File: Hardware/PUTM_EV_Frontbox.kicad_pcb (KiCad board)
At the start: 2 copper layers, 60 x 40 mm, 4 parts

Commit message: Initial layout, changes in safety sensing bus labels
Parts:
- added C1: 22uF, Capacitor_SMD:CP_Elec_4x5.8, F.Cu at (136.1, 99.9)
- added C10: 22uF, Capacitor_SMD:C_0805_2012Metric, F.Cu at (132.1, 116.9)
- added C11: 1uF, Capacitor_SMD:C_0603_1608Metric_Pad1.08x0.95mm_HandSolder, F.Cu at (141.6, 119.4)
- added C12: 1uF, Capacitor_SMD:C_0603_1608Metric_Pad1.08x0.95mm_HandSolder, F.Cu at (150.6, 119.4)
- added C13: 1uF, Capacitor_SMD:C_0603_1608Metric_Pad1.08x0.95mm_HandSolder, F.Cu at (151.1, 115.4)
- added C14: 1uF, Capacitor_SMD:C_0603_1608Metric_Pad1.08x0.95mm_HandSolder, F.Cu at (152.5, 108.4)
- added C15: 1uF, Capacitor_SMD:C_0603_1608Metric_Pad1.08x0.95mm_HandSolder, F.Cu at (156.1, 108.4)
- added C16: 1uF, Capacitor_SMD:C_0603_1608Metric_Pad1.08x0.95mm_HandSolder, F.Cu at (156.1, 115.4)
- added C17: 1uF, Capacitor_SMD:C_0603_1608Metric_Pad1.08x0.95mm_HandSolder, F.Cu at (147.0, 106.4)
- added C18: 1uF, Capacitor_SMD:C_0603_1608Metric_Pad1.08x0.95mm_HandSolder, F.Cu at (158.6, 105.4)
- added C19: 10u, Capacitor_SMD:C_0805_2012Metric_Pad1.18x1.45mm_HandSolder, F.Cu at (99.9, 138.8)
- added C2: 22uF, Capacitor_SMD:CP_Elec_4x5.8, F.Cu at (136.1, 105.4)
- added C20: 100nF, Capacitor_SMD:C_0603_1608Metric_Pad1.08x0.95mm_HandSolder, F.Cu at (117.9, 127.3)
- added C21: 100nF, Capacitor_SMD:C_0603_1608Metric_Pad1.08x0.95mm_HandSolder, F.Cu at (118.0, 140.8)
- added C22: 100nF, Capacitor_SMD:C_0603_1608Metric_Pad1.08x0.95mm_HandSolder, F.Cu at (115.0, 141.3)
- added C23: 100nF, Capacitor_SMD:C_0603_1608Metric_Pad1.08x0.95mm_HandSolder, F.Cu at (103.9, 139.8)
- added C24: 100nF, Capacitor_SMD:C_0603_1608Metric_Pad1.08x0.95mm_HandSolder, F.Cu at (102.9, 126.3)
- added C25: 100nF, Capacitor_SMD:C_0603_1608Metric_Pad1.08x0.95mm_HandSolder, F.Cu at (102.9, 124.3)
- added C26: 100nF, Capacitor_SMD:C_0603_1608Metric_Pad1.08x0.95mm_HandSolder, F.Cu at (110.5, 123.4)
- added C27: 100n, Capacitor_SMD:C_0603_1608Metric, F.Cu at (121.0, 132.1)
- added C28: 100nF, Capacitor_SMD:C_0603_1608Metric_Pad1.08x0.95mm_HandSolder, F.Cu at (123.3, 139.3)
- added C29: 6p, Capacitor_SMD:C_0603_1608Metric_Pad1.08x0.95mm_HandSolder, F.Cu at (119.8, 139.3)
- added C3: 100nF, Capacitor_SMD:C_0603_1608Metric, F.Cu at (137.6, 113.9)
- added C30: 100n, Capacitor_SMD:C_0603_1608Metric_Pad1.08x0.95mm_HandSolder, F.Cu at (100.8, 118.8)
- added C31: 100n, Capacitor_SMD:C_0603_1608Metric_Pad1.08x0.95mm_HandSolder, F.Cu at (108.6, 118.8)
- added C32: 47u, Capacitor_SMD:C_0603_1608Metric_Pad1.08x0.95mm_HandSolder, F.Cu at (100.8, 116.8)
- added C33: 10n, Capacitor_SMD:C_0603_1608Metric_Pad1.08x0.95mm_HandSolder, F.Cu at (108.6, 116.8)
- added C34: 47u, Capacitor_SMD:C_0603_1608Metric_Pad1.08x0.95mm_HandSolder, F.Cu at (106.1, 100.8)
- added C35: 220n, Capacitor_SMD:C_0603_1608Metric_Pad1.08x0.95mm_HandSolder, F.Cu at (102.8, 102.8)
- added C36: 100n, Capacitor_SMD:C_0603_1608Metric_Pad1.08x0.95mm_HandSolder, F.Cu at (108.8, 101.8)
- added C37: 10n, Capacitor_SMD:C_0603_1608Metric_Pad1.08x0.95mm_HandSolder, F.Cu at (106.1, 98.8)
- added C38: 100n, Capacitor_SMD:C_0603_1608Metric_Pad1.08x0.95mm_HandSolder, F.Cu at (117.7, 118.7)
- added C39: 100n, Capacitor_SMD:C_0603_1608Metric_Pad1.08x0.95mm_HandSolder, F.Cu at (124.7, 118.7)
- added C4: 22uF, Capacitor_SMD:C_0805_2012Metric, F.Cu at (142.6, 104.9)
- added C40: 47u, Capacitor_SMD:C_0603_1608Metric_Pad1.08x0.95mm_HandSolder, F.Cu at (117.7, 116.7)
- added C41: 10n, Capacitor_SMD:C_0603_1608Metric_Pad1.08x0.95mm_HandSolder, F.Cu at (124.7, 116.7)
- added C42: 47u, Capacitor_SMD:C_0603_1608Metric_Pad1.08x0.95mm_HandSolder, F.Cu at (122.0, 100.7)
- added C43: 220n, Capacitor_SMD:C_0603_1608Metric_Pad1.08x0.95mm_HandSolder, F.Cu at (118.5, 102.7)
- added C44: 100n, Capacitor_SMD:C_0603_1608Metric_Pad1.08x0.95mm_HandSolder, F.Cu at (124.7, 101.7)
- added C45: 10n, Capacitor_SMD:C_0603_1608Metric_Pad1.08x0.95mm_HandSolder, F.Cu at (122.0, 98.7)
- added C46: 100n, Capacitor_SMD:C_0603_1608Metric_Pad1.08x0.95mm_HandSolder, F.Cu at (91.8, 106.4)
- added C47: 100n, Capacitor_SMD:C_0603_1608Metric_Pad1.08x0.95mm_HandSolder, F.Cu at (91.8, 108.4)
- added C48: 100n, Capacitor_SMD:C_0603_1608Metric_Pad1.08x0.95mm_HandSolder, F.Cu at (91.8, 112.4)
- added C49: 10n, Capacitor_SMD:C_0603_1608Metric_Pad1.08x0.95mm_HandSolder, F.Cu at (80.8, 109.4)
- added C5: 22uF, Capacitor_SMD:C_0805_2012Metric, F.Cu at (142.6, 106.9)
- added C50: 100n, Capacitor_SMD:C_0603_1608Metric_Pad1.08x0.95mm_HandSolder, F.Cu at (91.4, 118.4)
- added C51: 100n, Capacitor_SMD:C_0603_1608Metric_Pad1.08x0.95mm_HandSolder, F.Cu at (91.4, 120.4)
- added C52: 100n, Capacitor_SMD:C_0603_1608Metric_Pad1.08x0.95mm_HandSolder, F.Cu at (91.4, 124.4)
- added C53: 10n, Capacitor_SMD:C_0603_1608Metric_Pad1.08x0.95mm_HandSolder, F.Cu at (80.5, 121.4)
- added C54: 100n, Capacitor_SMD:C_0603_1608Metric_Pad1.08x0.95mm_HandSolder, F.Cu at (78.8, 135.8)
- added C55: 100n, Capacitor_SMD:C_0603_1608Metric_Pad1.08x0.95mm_HandSolder, F.Cu at (82.8, 128.8)
- added C56: 100n, Capacitor_SMD:C_0603_1608Metric_Pad1.08x0.95mm_HandSolder, F.Cu at (82.8, 135.8)
- added C57: 100n, Capacitor_SMD:C_0603_1608Metric_Pad1.08x0.95mm_HandSolder, F.Cu at (131.8, 142.4)
- added C58: 100n, Capacitor_SMD:C_0603_1608Metric_Pad1.08x0.95mm_HandSolder, F.Cu at (145.9, 142.5)
- added C59: 100n, Capacitor_SMD:C_0603_1608Metric_Pad1.08x0.95mm_HandSolder, F.Cu at (134.8, 142.4)
- added C6: 100nF, Capacitor_SMD:C_0603_1608Metric, F.Cu at (142.3, 108.9)
- added C60: 100n, Capacitor_SMD:C_0603_1608Metric_Pad1.08x0.95mm_HandSolder, F.Cu at (148.9, 142.5)
- added C61: 100n, Capacitor_SMD:C_0603_1608Metric_Pad1.08x0.95mm_HandSolder, F.Cu at (137.8, 142.4)
- added C62: 100n, Capacitor_SMD:C_0603_1608Metric_Pad1.08x0.95mm_HandSolder, F.Cu at (151.9, 142.5)
- added C63: 100n, Capacitor_SMD:C_0603_1608Metric_Pad1.08x0.95mm_HandSolder, F.Cu at (140.8, 142.4)
- added C64: 100n, Capacitor_SMD:C_0603_1608Metric_Pad1.08x0.95mm_HandSolder, F.Cu at (154.9, 142.5)
- added C65: 100n, Capacitor_SMD:C_0603_1608Metric_Pad1.08x0.95mm_HandSolder, F.Cu at (137.8, 147.6)
- added C7: 22uF, Capacitor_SMD:C_0805_2012Metric, F.Cu at (139.6, 116.9)
- added C8: 22uF, Capacitor_SMD:C_0805_2012Metric, F.Cu at (137.1, 116.9)
- added C9: 22uF, Capacitor_SMD:C_0805_2012Metric, F.Cu at (134.6, 116.9)
- added D1: NSVRB751V40T1G, Diode_SMD:D_SOD-323_HandSoldering, F.Cu at (136.2, 167.0)
- added D10: 30V, Diode_SMD:D_SOD-123, F.Cu at (153.1, 99.9)
- added D11: LED, LED_SMD:LED_0603_1608Metric_Pad1.05x0.95mm_HandSolder, F.Cu at (94.5, 134.3)
- added D12: LED, LED_SMD:LED_0603_1608Metric_Pad1.05x0.95mm_HandSolder, F.Cu at (94.5, 132.8)
- added D13: LED, LED_SMD:LED_0603_1608Metric_Pad1.05x0.95mm_HandSolder, F.Cu at (94.5, 131.3)
- added D14: LED, LED_SMD:LED_0603_1608Metric_Pad1.05x0.95mm_HandSolder, F.Cu at (94.5, 129.8)
- added D2: 3.6V/400W, Package_TO_SOT_SMD:SOT-23-6, F.Cu at (90.9, 146.7)
- added D3: BZX84C5V6, Package_TO_SOT_SMD:SOT-23, F.Cu at (142.3, 123.3)
- added D4: BZX84C3V6-E3-08, Package_TO_SOT_SMD:SOT-23, F.Cu at (153.3, 119.8)
- added D5: 3.6V/400W, Package_TO_SOT_SMD:SOT-23-6, F.Cu at (87.4, 95.8)
- added D6: 5.3V/400W, Package_TO_SOT_SMD:SOT-23-3, F.Cu at (93.8, 96.3)
- added D7: 5.3V/400W, Package_TO_SOT_SMD:SOT-23-3, F.Cu at (127.2, 99.7)
- added D8: 5.3V/400W, Package_TO_SOT_SMD:SOT-23-3, F.Cu at (111.3, 99.6)
- added D9: 10V, Diode_SMD:D_SOD-123, F.Cu at (141.6, 100.9)
- added F1: 1.5A, Fuse:Fuse_1812_4532Metric, F.Cu at (149.6, 99.4)
- added F2: 300mA, Fuse:Fuse_0603_1608Metric_Pad1.05x0.95mm_HandSolder, F.Cu at (143.6, 119.4)
- added F3: 300mA, Fuse:Fuse_0603_1608Metric_Pad1.05x0.95mm_HandSolder, F.Cu at (149.1, 115.4)
- added F4: 300mA, Fuse:Fuse_0603_1608Metric_Pad1.05x0.95mm_HandSolder, F.Cu at (154.1, 115.4)
- added F5: 300mA, Fuse:Fuse_0603_1608Metric_Pad1.05x0.95mm_HandSolder, F.Cu at (150.6, 106.4)
- added F6: 300mA, Fuse:Fuse_0603_1608Metric_Pad1.05x0.95mm_HandSolder, F.Cu at (134.0, 113.9)
- added FB1: 2K@100MHz, Inductor_SMD:L_0603_1608Metric_Pad1.05x0.95mm_HandSolder, F.Cu at (103.8, 117.8)
- added FB2: 2K@100MHz, Inductor_SMD:L_0603_1608Metric_Pad1.05x0.95mm_HandSolder, F.Cu at (105.8, 117.8)
- added FB3: 2K@100MHz, Inductor_SMD:L_0603_1608Metric_Pad1.05x0.95mm_HandSolder, F.Cu at (106.1, 102.8)
- added FB4: 2K@100MHz, Inductor_SMD:L_0603_1608Metric_Pad1.05x0.95mm_HandSolder, F.Cu at (102.8, 100.8)
- added FB5: 2K@100MHz, Inductor_SMD:L_0603_1608Metric_Pad1.05x0.95mm_HandSolder, F.Cu at (120.2, 117.7)
- added FB6: 2K@100MHz, Inductor_SMD:L_0603_1608Metric_Pad1.05x0.95mm_HandSolder, F.Cu at (122.2, 117.7)
- added FB7: 2K@100MHz, Inductor_SMD:L_0603_1608Metric_Pad1.05x0.95mm_HandSolder, F.Cu at (122.0, 102.7)
- added FB8: 2K@100MHz, Inductor_SMD:L_0603_1608Metric_Pad1.05x0.95mm_HandSolder, F.Cu at (118.5, 100.7)
- added IC1: TPS54202HDDCR, Package_TO_SOT_SMD:SOT-23-6, F.Cu at (138.2, 111.4)
- added J1: XIAO ESP32S3 Sense, Samacsys:XIAO-ESP32S3-DIP, F.Cu at (121.6, 174.6)
- added J2: Conn_02x16_Counter_Clockwise, Connector_IDC:IDC-Header_2x17-1MP_P2.54mm_Latch6.5mm_Vertical, F.Cu at (90.7, 89.0)
- added J3: FTSH-107-01-L-D-K, Samacsys:FTSH-107-XX-YYY-D-K, F.Cu at (99.7, 146.9)
- added JP1: Jumper_2_Small_Bridged, Jumper:SolderJumper-2_P1.3mm_Open_TrianglePad1.0x1.5mm, F.Cu at (117.5, 95.3)
- added JP2: Jumper_2_Small_Bridged, Jumper:SolderJumper-2_P1.3mm_Open_TrianglePad1.0x1.5mm, F.Cu at (123.0, 131.8)
- added L1: 68uH/1.4A, Inductor_SMD:L_TDK_VLS6045EX_VLS6045AF, F.Cu at (144.5, 113.5)
- added Q1: SI2347DS-T1-GE3, Package_TO_SOT_SMD:SOT-23-3, F.Cu at (145.1, 100.9)
- added R1: 100k, Resistor_SMD:R_0603_1608Metric_Pad0.98x0.95mm_HandSolder, F.Cu at (142.6, 97.4)
- added R10: 1K, Resistor_SMD:R_0603_1608Metric_Pad0.98x0.95mm_HandSolder, F.Cu at (98.5, 134.3)
- added R11: 1K, Resistor_SMD:R_0603_1608Metric_Pad0.98x0.95mm_HandSolder, F.Cu at (98.5, 132.8)
- added R12: 1K, Resistor_SMD:R_0603_1608Metric_Pad0.98x0.95mm_HandSolder, F.Cu at (98.5, 131.3)
- added R13: 1K, Resistor_SMD:R_0603_1608Metric_Pad0.98x0.95mm_HandSolder, F.Cu at (98.5, 129.8)
- added R14: 100K, Resistor_SMD:R_0603_1608Metric_Pad0.98x0.95mm_HandSolder, F.Cu at (113.3, 102.8)
- added R15: 100K, Resistor_SMD:R_0603_1608Metric_Pad0.98x0.95mm_HandSolder, F.Cu at (129.7, 102.7)
- added R16: 330R, Resistor_SMD:R_0603_1608Metric_Pad0.98x0.95mm_HandSolder, F.Cu at (91.3, 103.5)
- added R17: 100k, Resistor_SMD:R_0603_1608Metric_Pad0.98x0.95mm_HandSolder, F.Cu at (78.8, 109.4)
- added R18: 0R, Resistor_SMD:R_0603_1608Metric_Pad0.98x0.95mm_HandSolder, F.Cu at (89.3, 103.5)
- added R19: 1K, Resistor_SMD:R_0603_1608Metric_Pad0.98x0.95mm_HandSolder, F.Cu at (93.3, 103.5)
- added R2: 510k, Resistor_SMD:R_0603_1608Metric, F.Cu at (139.1, 108.9)
- added R20: 1K, Resistor_SMD:R_0603_1608Metric_Pad0.98x0.95mm_HandSolder, F.Cu at (91.8, 110.4)
- added R21: 1K, Resistor_SMD:R_0603_1608Metric_Pad0.98x0.95mm_HandSolder, F.Cu at (79.8, 104.4)
- added R22: 1k, Resistor_SMD:R_0603_1608Metric_Pad0.98x0.95mm_HandSolder, F.Cu at (79.8, 106.4)
- added R23: 300R, Resistor_SMD:R_0603_1608Metric_Pad0.98x0.95mm_HandSolder, F.Cu at (90.5, 115.4)
- added R24: 100k, Resistor_SMD:R_0603_1608Metric_Pad0.98x0.95mm_HandSolder, F.Cu at (78.5, 121.4)
- added R25: 0R, Resistor_SMD:R_0603_1608Metric_Pad0.98x0.95mm_HandSolder, F.Cu at (88.5, 115.4)
- added R26: 0R, Resistor_SMD:R_0603_1608Metric_Pad0.98x0.95mm_HandSolder, F.Cu at (92.5, 115.4)
- added R27: 1K, Resistor_SMD:R_0603_1608Metric_Pad0.98x0.95mm_HandSolder, F.Cu at (91.4, 122.4)
- added R28: 1K, Resistor_SMD:R_0603_1608Metric_Pad0.98x0.95mm_HandSolder, F.Cu at (79.5, 116.4)
- added R29: 1K, Resistor_SMD:R_0603_1608Metric_Pad0.98x0.95mm_HandSolder, F.Cu at (79.5, 118.4)
- added R3: 100k, Resistor_SMD:R_0603_1608Metric, F.Cu at (134.4, 112.4)
- added R30: 1K, Resistor_SMD:R_0603_1608Metric_Pad0.98x0.95mm_HandSolder, F.Cu at (78.8, 137.8)
- added R31: 100K, Resistor_SMD:R_0603_1608Metric_Pad0.98x0.95mm_HandSolder, F.Cu at (78.8, 139.8)
- added R32: 1K, Resistor_SMD:R_0603_1608Metric_Pad0.98x0.95mm_HandSolder, F.Cu at (82.8, 137.8)
- added R33: 100K, Resistor_SMD:R_0603_1608Metric_Pad0.98x0.95mm_HandSolder, F.Cu at (82.8, 139.8)
- added R34: 10k, Resistor_SMD:R_0603_1608Metric_Pad0.98x0.95mm_HandSolder, F.Cu at (131.8, 128.8)
- added R35: 10k, Resistor_SMD:R_0603_1608Metric_Pad0.98x0.95mm_HandSolder, F.Cu at (145.4, 129.0)
- added R36: 2k, Resistor_SMD:R_0603_1608Metric_Pad0.98x0.95mm_HandSolder, F.Cu at (130.3, 142.4)
- added R37: 2k, Resistor_SMD:R_0603_1608Metric_Pad0.98x0.95mm_HandSolder, F.Cu at (144.4, 142.5)
- added R38: 10k, Resistor_SMD:R_0603_1608Metric_Pad0.98x0.95mm_HandSolder, F.Cu at (134.3, 128.8)
- added R39: 10k, Resistor_SMD:R_0603_1608Metric_Pad0.98x0.95mm_HandSolder, F.Cu at (147.9, 129.0)
- added R4: 43k, Resistor_SMD:R_0603_1608Metric, F.Cu at (136.1, 108.9)
- added R40: 2k, Resistor_SMD:R_0603_1608Metric_Pad0.98x0.95mm_HandSolder, F.Cu at (133.3, 142.4)
- added R41: 2k, Resistor_SMD:R_0603_1608Metric_Pad0.98x0.95mm_HandSolder, F.Cu at (147.4, 142.5)
- added R42: 10k, Resistor_SMD:R_0603_1608Metric_Pad0.98x0.95mm_HandSolder, F.Cu at (136.8, 128.8)
- added R43: 10k, Resistor_SMD:R_0603_1608Metric_Pad0.98x0.95mm_HandSolder, F.Cu at (150.4, 129.0)
- added R44: 2k, Resistor_SMD:R_0603_1608Metric_Pad0.98x0.95mm_HandSolder, F.Cu at (136.3, 142.4)
- added R45: 2k, Resistor_SMD:R_0603_1608Metric_Pad0.98x0.95mm_HandSolder, F.Cu at (150.4, 142.5)
- added R46: 10k, Resistor_SMD:R_0603_1608Metric_Pad0.98x0.95mm_HandSolder, F.Cu at (139.3, 128.9)
- added R47: 10k, Resistor_SMD:R_0603_1608Metric_Pad0.98x0.95mm_HandSolder, F.Cu at (152.9, 129.0)
- added R48: 2k, Resistor_SMD:R_0603_1608Metric_Pad0.98x0.95mm_HandSolder, F.Cu at (139.2, 142.4)
- added R49: 2k, Resistor_SMD:R_0603_1608Metric_Pad0.98x0.95mm_HandSolder, F.Cu at (153.4, 142.5)
- added R5: 13.3k, Resistor_SMD:R_0603_1608Metric, F.Cu at (134.4, 110.9)
- added R50: 10k, Resistor_SMD:R_0603_1608Metric_Pad0.98x0.95mm_HandSolder, F.Cu at (149.8, 147.8)
- added R51: 2k, Resistor_SMD:R_0603_1608Metric_Pad0.98x0.95mm_HandSolder, F.Cu at (135.3, 147.6)
- added R6: 1k, Resistor_SMD:R_0603_1608Metric, F.Cu at (112.5, 123.4)
- added R7: 10k, Resistor_SMD:R_0603_1608Metric, F.Cu at (119.0, 132.1)
- added R8: 10k, Resistor_SMD:R_0603_1608Metric, F.Cu at (112.4, 142.3)
- added R9: 10k, Resistor_SMD:R_0603_1608Metric, F.Cu at (112.4, 144.3)
- added TP1: TestPoint_Small, TestPoint:TestPoint_THTPad_D1.0mm_Drill0.5mm, F.Cu at (139.6, 97.4)
- added TP10: APPS_MID, TestPoint:TestPoint_THTPad_D1.0mm_Drill0.5mm, F.Cu at (73.8, 133.3)
- added TP11: BRAKE_OUT, TestPoint:TestPoint_THTPad_D1.0mm_Drill0.5mm, F.Cu at (73.8, 130.3)
- added TP12: BRAKE_MID, TestPoint:TestPoint_THTPad_D1.0mm_Drill0.5mm, F.Cu at (87.8, 133.3)
- added TP13: BRAKE_OUT, TestPoint:TestPoint_THTPad_D1.0mm_Drill0.5mm, F.Cu at (87.8, 130.3)
- added TP2: TestPoint_Small, TestPoint:TestPoint_THTPad_D1.0mm_Drill0.5mm, F.Cu at (149.5, 108.4)
- added TP3: TestPoint_Small, TestPoint:TestPoint_THTPad_D1.0mm_Drill0.5mm, F.Cu at (114.9, 124.3)
- added TP4: APPS_P, TestPoint:TestPoint_THTPad_D1.0mm_Drill0.5mm, F.Cu at (75.8, 109.4)
- added TP5: APPS_OUT, TestPoint:TestPoint_THTPad_D1.0mm_Drill0.5mm, F.Cu at (95.8, 108.4)
- added TP6: APPS_N, TestPoint:TestPoint_THTPad_D1.0mm_Drill0.5mm, F.Cu at (75.8, 106.9)
- added TP7: APPS_P, TestPoint:TestPoint_THTPad_D1.0mm_Drill0.5mm, F.Cu at (75.5, 121.9)
- added TP8: APPS_OUT, TestPoint:TestPoint_THTPad_D1.0mm_Drill0.5mm, F.Cu at (95.5, 120.4)
- added TP9: APPS_N, TestPoint:TestPoint_THTPad_D1.0mm_Drill0.5mm, F.Cu at (75.5, 118.9)
- added U1: TLV743P, Package_TO_SOT_SMD:SOT-23-5_HandSoldering, F.Cu at (146.9, 119.5)
- added U10: MCP6N11-001E/SN, Package_SO:SOIC-8_3.9x4.9mm_P1.27mm, F.Cu at (85.5, 120.4)
- added U11: MCP6002-xSN, Package_SO:SOIC-8_3.9x4.9mm_P1.27mm, F.Cu at (80.8, 132.3)
- added U12: TLP291-4, Package_SO:SOIC-16_4.55x10.3mm_P1.27mm, F.Cu at (136.3, 135.8)
- added U13: TLP291-4, Package_SO:SOIC-16_4.55x10.3mm_P1.27mm, F.Cu at (150.3, 135.8)
- added U14: FODM217B, Package_SO:SOP-4_4.4x2.6mm_P1.27mm, F.Cu at (143.8, 147.8)
- added U2: TLV743P, Package_TO_SOT_SMD:SOT-23-5_HandSoldering, F.Cu at (151.2, 111.4)
- added U3: TLV743P, Package_TO_SOT_SMD:SOT-23-5_HandSoldering, F.Cu at (156.6, 111.5)
- added U4: TLV743P, Package_TO_SOT_SMD:SOT-23-5_HandSoldering, F.Cu at (154.9, 105.5)
- added U5: LM4040C33FTA, Package_TO_SOT_SMD:SOT-23, F.Cu at (107.4, 123.2)
- added U6: STM32G484RETx, Package_QFP:LQFP-64_10x10mm_P0.5mm, F.Cu at (110.0, 133.8)
- added U7: ADM3057ExRW, Package_SO:SOIC-20W_7.5x12.8mm_P1.27mm, F.Cu at (107.8, 109.8)
- added U8: ADM3057ExRW, Package_SO:SOIC-20W_7.5x12.8mm_P1.27mm, F.Cu at (123.7, 109.7)
- added U9: MCP6N11-001E/SN, Package_SO:SOIC-8_3.9x4.9mm_P1.27mm, F.Cu at (85.8, 108.4)
- added Y1: ATX-11-F-32.000MHZ-F05-T, Samacsys:ATX11F32000MHZF05T, F.Cu at (121.4, 136.0)
- moved REF** 105.1 mm to (81.2, 26.4)
- moved REF** 105.1 mm to (31.2, 56.4)
- moved REF** 105.1 mm to (31.2, 26.4)
- moved REF** 105.1 mm to (81.2, 56.4)
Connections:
- REF** pad 1: (no net) -> GND (x4)
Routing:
- net /CAN bus/GND_CAN_ISO2: track 0.00 -> 26.8 mm
- net /CAN bus/GND_CAN_ISO1: track 0.00 -> 24.3 mm
- net Net-(R20-Pad1): track 0.00 -> 15.1 mm
- net Net-(R27-Pad1): track 0.00 -> 14.9 mm
- net /APPS2_SUPPLY: track 0.00 -> 11.3 mm
- net /APPS1_SUPPLY: track 0.00 -> 11.2 mm
- net Net-(U11A-+): track 0.00 -> 10.4 mm
- net Net-(C43-Pad1): track 0.00 -> 9.58 mm
- net Net-(C35-Pad1): track 0.00 -> 9.54 mm
- net Net-(U11B-+): track 0.00 -> 8.68 mm
- net /APPS_POT_2: track 0.00 -> 8.64 mm
- net /DAC2_REF: track 0.00 -> 8.52 mm
- net /DAC1_REF: track 0.00 -> 8.52 mm
- net /APPS_POT_1: track 0.00 -> 8.38 mm
- net Net-(U7-VISOIN): track 0.00 -> 8.26 mm
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
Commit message: Initial routing (Piotruś proszę nie bij że brzydko)
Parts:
- added D15: 3.6V/400W, Package_TO_SOT_SMD:SOT-23-6, F.Cu at (93.5, 143.2)
- C30, C38: value 100n -> 47u; footprint Capacitor_SMD:C_0603_1608Metric_Pad1.08x0.95mm_HandSolder -> Capacitor_SMD:C_0805_2012Metric_Pad1.18x1.45mm_HandSolder
- C32, C34, C40, C42: footprint Capacitor_SMD:C_0603_1608Metric_Pad1.08x0.95mm_HandSolder -> Capacitor_SMD:C_0805_2012Metric_Pad1.18x1.45mm_HandSolder
- C35, C43: value 220n -> 47u; footprint Capacitor_SMD:C_0603_1608Metric_Pad1.08x0.95mm_HandSolder -> Capacitor_SMD:C_0805_2012Metric_Pad1.18x1.45mm_HandSolder
- D7, D8: value 5.3V/400W -> PESD5V0L2BT; footprint Package_TO_SOT_SMD:SOT-23-3 -> Package_TO_SOT_SMD:SOT-23_Handsoldering
- moved REF** 129.3 mm to (162.4, 157.0)
- moved REF** 107.3 mm to (68.5, 157.0)
- moved REF** 101.3 mm to (162.4, 86.9)
- moved C16 82.5 mm to (73.5, 116.1), turned to 180 degrees
- moved C18 80.9 mm to (83.0, 134.2), turned to 180 degrees
- moved F4 80.6 mm to (73.5, 114.1), turned to 0 degrees
- moved U4 79.2 mm to (82.3, 137.2)
- moved F5 79.2 mm to (78.0, 138.0)
- moved U3 79.2 mm to (77.5, 115.7), turned to -90 degrees
- moved C13 78.7 mm to (73.6, 101.7), turned to 180 degrees
- moved F3 77.1 mm to (73.6, 99.7), turned to 0 degrees
- moved C17 76.8 mm to (78.0, 140.0), turned to 0 degrees
- moved C15 75.9 mm to (80.5, 116.1), turned to 90 degrees
- moved U2 74.5 mm to (77.4, 101.2), turned to -90 degrees
- moved C14 72.3 mm to (80.5, 101.4), turned to 90 degrees
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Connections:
- net /MCU/UART_RX renamed /Connector/UART_RX
- net /MCU/UART_TX renamed /Connector/UART_TX
- D7 pad 1: /CAN bus/CAN2- -> /CAN bus/CAN2+
- D7 pad 2: /CAN bus/CAN2+ -> /CAN bus/CAN2-
- D8 pad 1: /CAN bus/CAN1- -> /CAN bus/CAN1+
- D8 pad 2: /CAN bus/CAN1+ -> /CAN bus/CAN1-
- J3 pad 13: unconnected-(J3-Pin_13-Pad13) -> /Connector/UART_RX_PROG
- J3 pad 14: unconnected-(J3-Pin_14-Pad14) -> /Connector/UART_TX_PROG
- U6 pad 30: unconnected-(U6-PB10-Pad30) -> /Connector/UART_RX_PROG
- U6 pad 9: unconnected-(U6-PC1-Pad9) -> /Connector/UART_TX_PROG
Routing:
- net +3.3V: track 2.05 -> 231.3 mm, vias 0 -> 12
- net +5V: track 2.19 -> 170.6 mm, vias 0 -> 8
- net /MCU/RIGHT_KILL_S: track 0.00 -> 84.7 mm, vias 0 -> 2
- net /Connector/RIGHT_KILL: track 0.00 -> 82.0 mm, vias 0 -> 1
- net /MCU/BSPD_S: track 0.00 -> 81.6 mm, vias 0 -> 2
- net /Connector/BSPD: track 0.00 -> 80.9 mm, vias 0 -> 1
- net /MCU/OVERTRAVEL_S: track 0.00 -> 80.8 mm, vias 0 -> 2
- net /Connector/LEFT_WHEEL: track 0.00 -> 79.3 mm, vias 0 -> 1
- net /Connector/RIGHT_WHEEL: track 0.00 -> 76.8 mm, vias 0 -> 1
- net /MCU/RIGHT_WHEEL_S: track 0.00 -> 76.7 mm, vias 0 -> 2
- net /Connector/OVERTRAVEL: track 0.00 -> 76.6 mm, vias 0 -> 1
- net /BRAKE_PRESSURE2_IN: track 2.76 -> 73.9 mm, vias 0 -> 2
- net /MCU/DRIVER_KILL_S: track 0.00 -> 66.8 mm, vias 0 -> 2
- net /MCU/LEFT_WHEEL_S: track 0.00 -> 66.1 mm, vias 0 -> 3
- net /BRAKE_PRESSURE1_IN: track 2.00 -> 67.7 mm, vias 0 -> 2
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- added copper zone on F.Cu, net +24V
- added copper zone on F.Cu, net +5V
- added copper zone on F.Cu, net /CAN bus/GND_CAN_ISO1
- added copper zone on F.Cu, net /CAN bus/GND_CAN_ISO2
- added copper zone on B.Cu, net GND
- added copper zone on F.Cu, net GND
- added copper zone on In1.Cu, net GND
- added copper zone on In2.Cu, net GND
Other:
- board outline removed
- copper layers 2 -> 4
- board text removed: "Template"
- board text removed: "v${REVISION}"

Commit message: Changes in CAN section
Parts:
- removed REF** (x4): MountingHole_3mm_Pad_Via, MountingHole:MountingHole_3mm_Pad_Via
- added C66: 4.7nF/Y2, Samacsys:CAPC5728X280N, F.Cu at (98.9, 100.0)
- added C67: 4.7nF/Y2, Samacsys:CAPC5728X280N, F.Cu at (132.3, 97.6)
- added FB10: 2K@100MHz, Inductor_SMD:L_0805_2012Metric_Pad1.05x1.20mm_HandSolder, F.Cu at (93.6, 122.0)
- FB1, FB2, FB3, FB4, FB5, FB6, FB7, FB8: footprint Inductor_SMD:L_0603_1608Metric_Pad1.05x0.95mm_HandSolder -> Inductor_SMD:L_0805_2012Metric_Pad1.05x1.20mm_HandSolder
- moved D4 60.5 mm to (99.1, 148.4), turned to 180 degrees
- moved J1 52.0 mm to (76.0, 133.7)
- moved JP1 33.2 mm to (135.5, 125.2), turned to 0 degrees
- moved D1 33.0 mm to (83.2, 145.5), turned to 0 degrees
- moved C63 28.4 mm to (126.0, 134.4)
- moved R48 28.4 mm to (127.5, 134.4)
- moved C57 28.4 mm to (135.0, 134.4)
- moved C59 28.4 mm to (132.0, 134.4)
- moved C61 28.4 mm to (129.0, 134.4)
- moved R34 28.4 mm to (135.0, 148.0)
- moved R36 28.4 mm to (136.5, 134.4)
- moved R38 28.4 mm to (132.5, 148.0)
- moved R40 28.4 mm to (133.5, 134.4)
- moved R42 28.4 mm to (130.0, 148.0)
- moved R44 28.4 mm to (130.5, 134.4)
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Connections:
- D3 pad 3: +5V -> /Connector/5V_EXT
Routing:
- net +5V: track 170.6 -> 11.2 mm, vias 8 -> 0
- net /MCU/RIGHT_KILL_S: track 84.7 -> 2.88 mm, vias 2 -> 0
- net /MCU/BSPD_S: track 81.6 -> 2.86 mm, vias 2 -> 0
- net /MCU/OVERTRAVEL_S: track 80.8 -> 2.89 mm, vias 2 -> 0
- net /MCU/RIGHT_WHEEL_S: track 76.7 -> 2.82 mm, vias 2 -> 0
- net /BRAKE_PRESSURE2_IN: track 73.9 -> 9.20 mm, vias 2 -> 0
- net /MCU/DRIVER_KILL_S: track 66.8 -> 2.74 mm, vias 2 -> 0
- net /MCU/LEFT_WHEEL_S: track 66.1 -> 2.93 mm, vias 3 -> 0
- net /CAN bus/CAN2_TX: track 63.0 -> 0.00 mm, vias 2 -> 0
- net /MCU/LEFT_KILL_S: track 65.2 -> 2.76 mm, vias 2 -> 0
- net /BRAKE_PRESSURE1_IN: track 67.7 -> 5.66 mm, vias 2 -> 0
- net /MCU/EBS_S: track 63.7 -> 2.78 mm, vias 2 -> 0
- net /CAN bus/CAN2_RX: track 59.1 -> 0.00 mm, vias 2 -> 0
- net /BRAKE_PRESSURE_FRONT_OUT: track 59.9 -> 1.27 mm, vias 1 -> 0
- net /MCU/INERTIA_S: track 61.3 -> 2.79 mm, vias 2 -> 0
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- added copper zone on B.Cu, net /CAN bus/GND_CAN_ISO1
- added copper zone on In1.Cu, net /CAN bus/GND_CAN_ISO1
- added copper zone on In2.Cu, net /CAN bus/GND_CAN_ISO1
- added copper zone on B.Cu, net /CAN bus/GND_CAN_ISO2
- added copper zone on In1.Cu, net /CAN bus/GND_CAN_ISO2
- added copper zone on In2.Cu, net /CAN bus/GND_CAN_ISO2
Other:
- board outline added: 97 x 70 mm

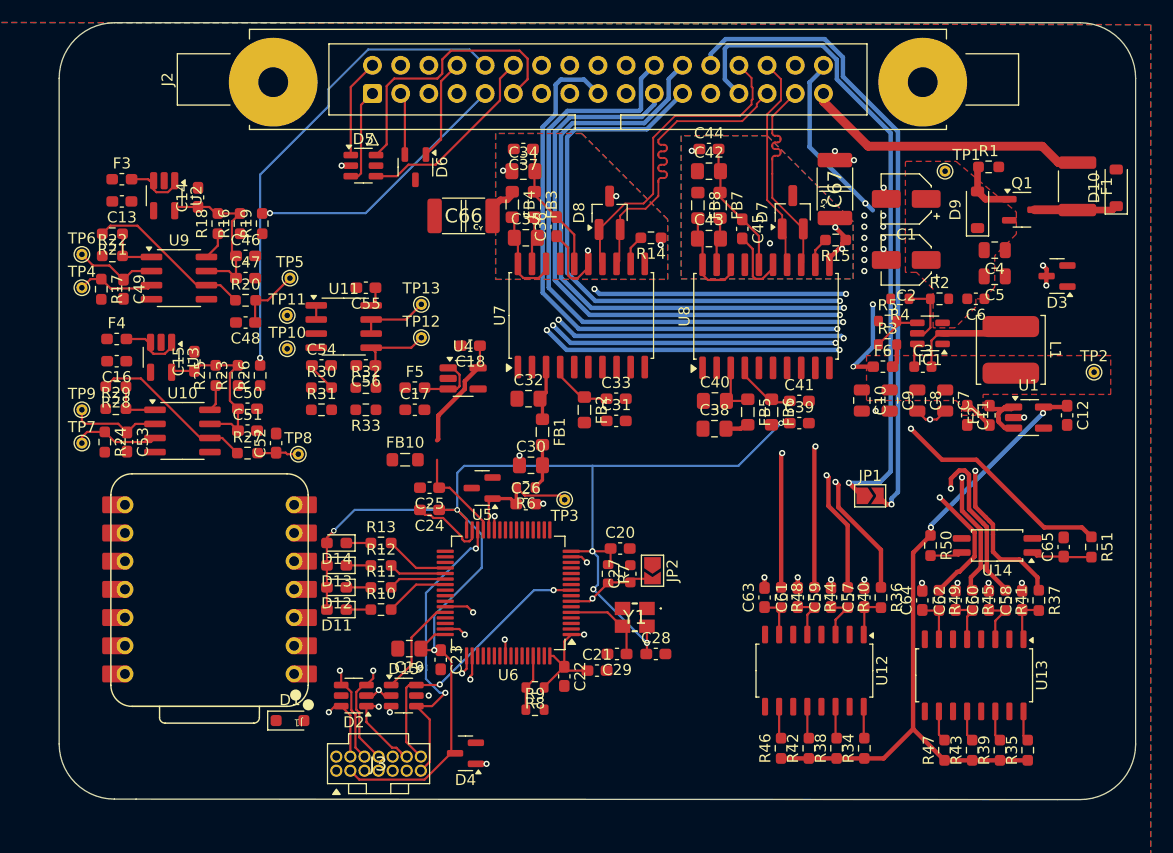
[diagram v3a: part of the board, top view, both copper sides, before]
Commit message: Changes in CAN filter section, updated routing
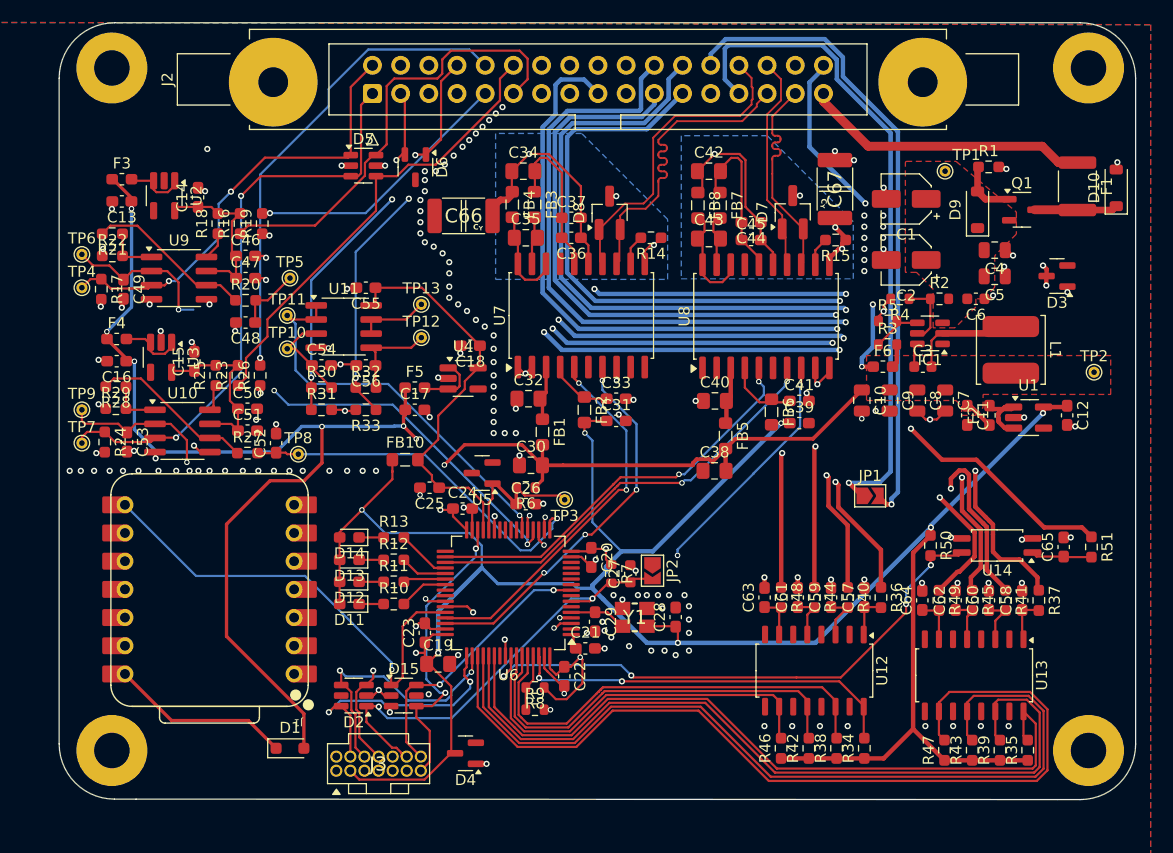
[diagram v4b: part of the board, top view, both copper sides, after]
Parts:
- added ?: , , F.Cu at (155.2, 148.2)
- added ?: , , F.Cu at (155.2, 86.7)
- added ?: , , F.Cu at (67.2, 86.7)
- added ?: , , F.Cu at (67.2, 148.2)
- moved C44 7.62 mm to (124.8, 100.6), turned to 180 degrees
- moved C37 7.56 mm to (108.6, 100.2), turned to 0 degrees
- moved C38 3.80 mm to (121.5, 123.0)
- moved C28 3.77 mm to (118.0, 136.2), turned to 90 degrees
- moved C29 3.51 mm to (110.7, 136.6), turned to -90 degrees
- moved C24 2.98 mm to (98.8, 126.4), turned to 0 degrees
- moved C19 2.94 mm to (96.6, 140.4), turned to 0 degrees
- moved FB5 2.94 mm to (122.5, 119.8)
- moved C23 2.81 mm to (95.4, 137.6), turned to 90 degrees
- moved C20 2.72 mm to (110.4, 130.8), turned to -90 degrees
- moved D1 2.50 mm to (83.2, 148.0)
- moved C21 2.26 mm to (109.9, 139.0)
- moved C36 1.66 mm to (108.6, 102.0), turned to 180 degrees
- moved U5 1.35 mm to (100.6, 123.2)
- moved C45 1.28 mm to (124.8, 102.2), turned to 0 degrees
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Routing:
- net +5V: track 11.2 -> 151.0 mm, vias 0 -> 7
- net +3.3V: track 201.0 -> 281.3 mm, vias 10 -> 11
- net /MCU/INERTIA_S: track 2.79 -> 82.5 mm
- net /MCU/EBS_S: track 2.78 -> 77.2 mm
- net /MCU/LEFT_KILL_S: track 2.76 -> 72.7 mm
- net /MCU/DRIVER_KILL_S: track 2.74 -> 66.6 mm
- net GND: track 27.4 -> 77.8 mm, vias 34 -> 178
- net /DAC1_REF: track 7.53 -> 56.1 mm, vias 0 -> 3
- net /MCU/LEFT_WHEEL_S: track 2.93 -> 50.6 mm, vias 0 -> 4
- net /DAC2_REF: track 8.34 -> 51.9 mm, vias 0 -> 2
- net /CAN bus/CAN2_TX: track 0.00 -> 38.9 mm, vias 0 -> 2
- net /CAN bus/CAN2_RX: track 0.00 -> 37.4 mm, vias 0 -> 2
- net /MCU/RIGHT_KILL_S: track 2.88 -> 39.8 mm
- net /APPS_POT_2: track 16.5 -> 53.2 mm, vias 0 -> 2
- net /CAN bus/STBY_CAN_2: track 0.00 -> 35.7 mm, vias 0 -> 3
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- removed copper zone on F.Cu, net /CAN bus/GND_CAN_ISO1
- removed copper zone on F.Cu, net /CAN bus/GND_CAN_ISO2
